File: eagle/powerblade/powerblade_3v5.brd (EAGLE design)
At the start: 25.4 x 25.4 mm, 78 parts, among them J1 JTAG_14PIN_IDC-ND, J2 AC_INFINAL, J4 TC2030-JLINK-NL, Q1 NTS4173, Q4 2SK1829, U1 TPS62122, U2 MCP6V3, U3 MSP430FR5738, U4 NRF51822QF, U6 MAX9910, U7 OPA2369, X1 16MHz, X3 32.768kHz, Y1 UREACH_XTEND

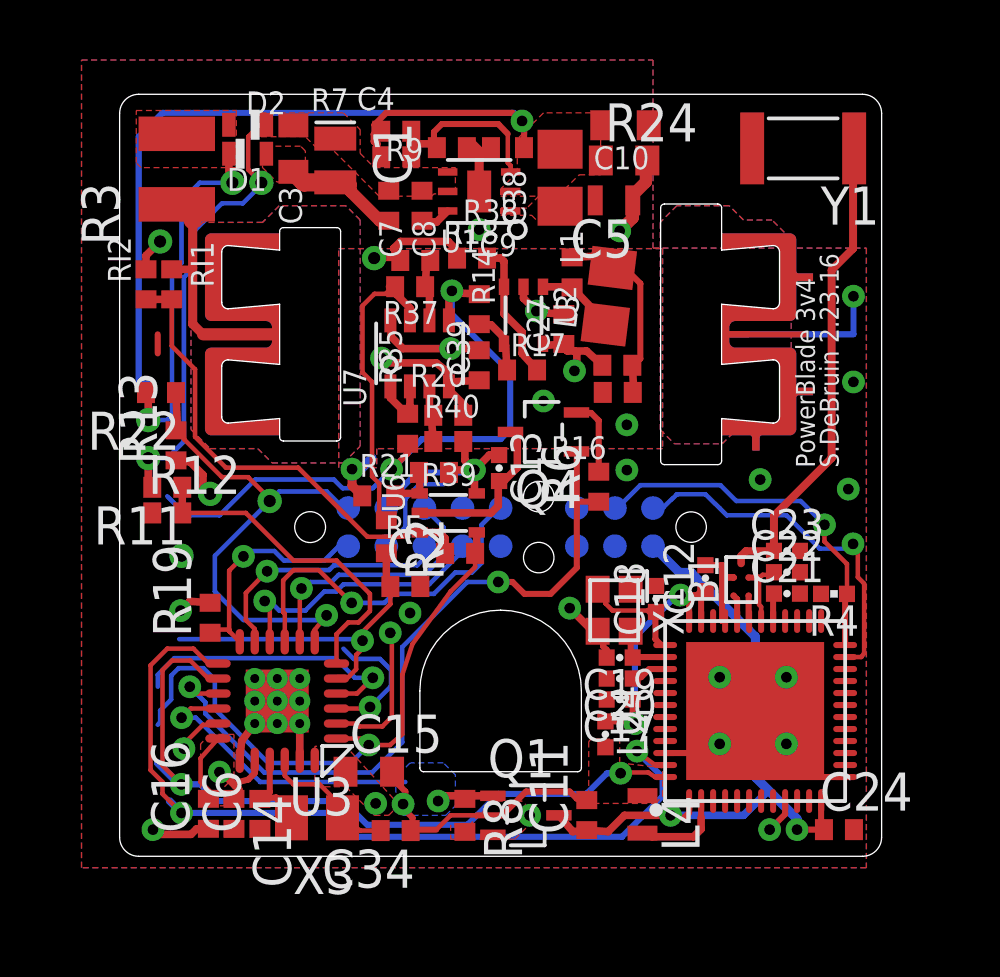
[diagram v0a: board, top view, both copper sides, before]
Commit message: cleaned up after removing header
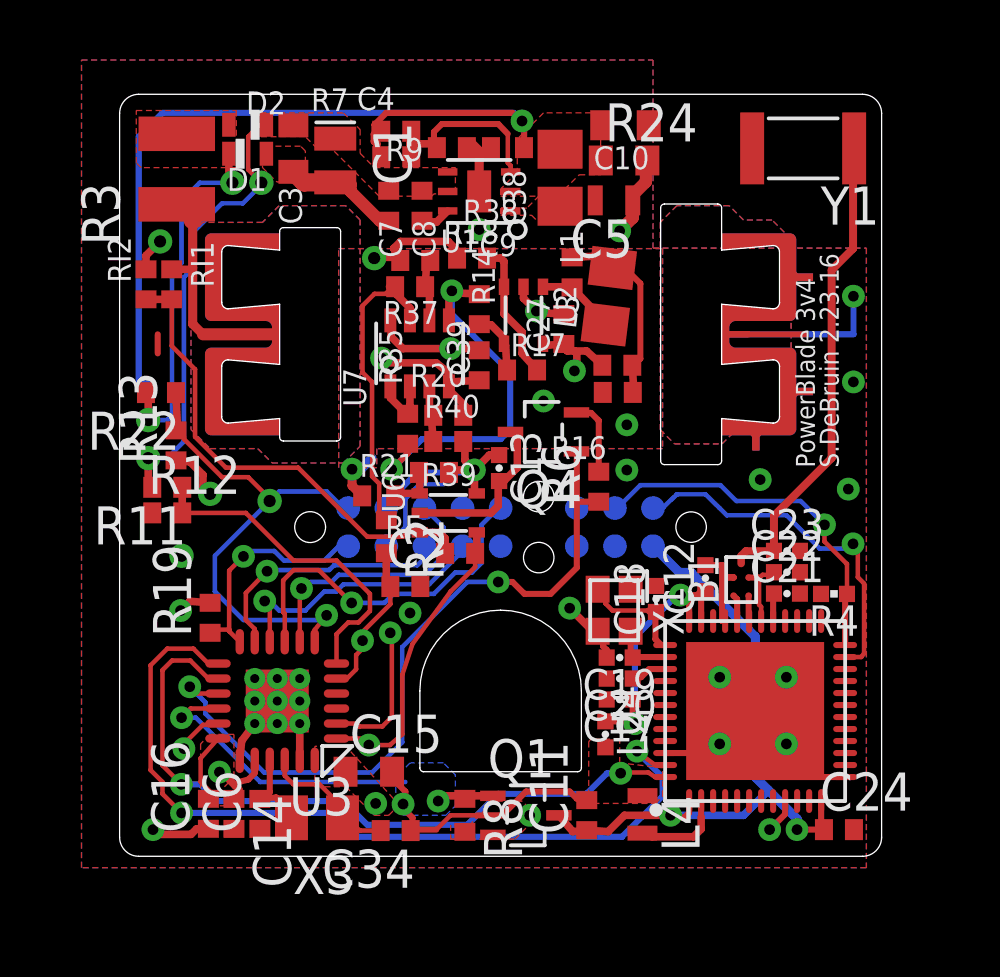
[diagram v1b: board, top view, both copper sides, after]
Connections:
- removed net PWM_CURRENT: U3.P3
- removed net PWM_VOLTAGE: U3.P4
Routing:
- net V_SENSE: track 20.6 -> 9.98 mm
- net PWM_VOLTAGE: track 9.49 -> 0.00 mm, vias 1 -> 0
- net VFILT: track 32.0 -> 23.4 mm
- net I_SENSE: track 11.3 -> 5.18 mm
- net PWM_CURRENT: track 4.54 -> 0.00 mm, vias 1 -> 0
- net FROMBLE_RX: track 24.8 -> 23.8 mm
- net TOBLE_TX: track 28.7 -> 28.1 mm
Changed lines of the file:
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@@
 <grid distance="25" unitdist="mil" unit="mil" style="lines" multiple="1" display="no" altdistance="3.125" altunitdist="mil" altunit="mil"/>
 <layers>
-<layer number="1" name="Top" color="4" fill="1" visible="yes" active="yes"/>
-<layer number="2" name="Route2" color="1" fill="3" visible="yes" active="yes"/>
+<layer number="1" name="Top" color="4" fill="1" visible="no" active="yes"/>
+<layer number="2" name="Route2" color="1" fill="3" visible="no" active="yes"/>
 <layer number="3" name="Route3" color="4" fill="3" visible="no" active="no"/>
 <layer number="4" name="Route4" color="1" fill="4" visible="no" active="no"/>
@@
 <layer number="13" name="Route13" color="4" fill="5" visible="no" active="no"/>
 <layer number="14" name="Route14" color="1" fill="6" visible="no" active="no"/>
-<layer number="15" name="Route15" color="4" fill="6" visible="yes" active="yes"/>
+<layer number="15" name="Route15" color="4" fill="6" visible="no" active="yes"/>
 <layer number="16" name="Bottom" color="1" fill="1" visible="yes" active="yes"/>
 <layer number="17" name="Pads" color="2" fill="1" visible="yes" active="yes"/>
@@
 <contactref element="RF" pad="2"/>
 <contactref element="U6" pad="P4"/>
-<wire x1="-11.43" y1="-13.0175" x2="-11.350625" y2="-12.938125" width="0.1524" layer="16"/>
-<wire x1="-11.350625" y1="-12.938125" x2="-11.350625" y2="-12.54125" width="0.1524" layer="16"/>
-<wire x1="-11.350625" y1="-12.54125" x2="-10.982325" y2="-12.17295" width="0.1524" layer="16"/>
-<wire x1="-10.982325" y1="-12.17295" x2="-10.982325" y2="-11.3792" width="0.1524" layer="16"/>
-<wire x1="-10.982325" y1="-11.3792" x2="-10.7299125" y2="-11.1267875" width="0.1524" layer="16"/>
 <via x="-4.3942" y="-13.69186875" extent="1-16" drill="0.3556"/>
-<wire x1="-4.3942" y1="-13.69186875" x2="-5.000625" y2="-14.2875" width="0.1524" layer="16"/>
-<wire x1="-5.000625" y1="-14.2875" x2="-7.750175" y2="-14.2875" width="0.1524" layer="16"/>
-<wire x1="-7.750175" y1="-14.2875" x2="-9.525" y2="-12.487275" width="0.1524" layer="16"/>
-<wire x1="-9.525" y1="-12.487275" x2="-9.525" y2="-11.509375" width="0.1524" layer="16"/>
-<wire x1="-9.525" y1="-11.509375" x2="-9.9075875" y2="-11.1267875" width="0.1524" layer="16"/>
-<wire x1="-9.9075875" y1="-11.1267875" x2="-10.7299125" y2="-11.1267875" width="0.1524" layer="16"/>
 <wire x1="-3.69061875" y1="-13.69186875" x2="-3.279775" y2="-13.335" width="0.1524" layer="1"/>
 <wire x1="-3.279775" y1="-13.335" x2="-3.279775" y2="-11.350625" width="0.1524" layer="1"/>
@@
 <wire x1="-3.0988" y1="-3.96875" x2="-3.6322" y2="-4.50215" width="0.2032" layer="1"/>
 <wire x1="-3.609975" y1="-4.524375" x2="-3.6322" y2="-4.50215" width="0.1524" layer="1"/>
-<wire x1="-3.6322" y1="-4.50215" x2="-4.26085" y2="-5.1308" width="0.1524" layer="16"/>
-<wire x1="-8.175625" y1="-4.841875" x2="-9.36625" y2="-6.0325" width="0.1524" layer="16"/>
-<wire x1="-9.36625" y1="-6.0325" x2="-10.4775" y2="-6.0325" width="0.1524" layer="16"/>
-<wire x1="-10.4775" y1="-6.0325" x2="-11.1125" y2="-5.3975" width="0.1524" layer="16"/>
-<wire x1="-4.26085" y1="-5.1308" x2="-5.267325" y2="-5.1308" width="0.1524" layer="16"/>
-<wire x1="-5.267325" y1="-5.1308" x2="-5.55625" y2="-4.841875" width="0.1524" layer="16"/>
-<wire x1="-5.55625" y1="-4.841875" x2="-8.175625" y2="-4.841875" width="0.1524" layer="16"/>
 <via x="-3.679825" y="-9.95045" extent="1-16" drill="0.3556"/>
 <contactref element="U3" pad="P2"/>
@@
 <wire x1="-4.816475" y1="-10.690225" x2="-4.60375" y2="-10.4775" width="0.1524" layer="1"/>
 <wire x1="-4.60375" y1="-10.4775" x2="-4.60375" y2="-10.2108" width="0.1524" layer="1"/>
-<wire x1="-10.715625" y1="-10.16" x2="-4.65455" y2="-10.16" width="0.1524" layer="16"/>
-<wire x1="-4.65455" y1="-10.16" x2="-4.60375" y2="-10.2108" width="0.1524" layer="16"/>
 <wire x1="-3.675" y1="-8.4074" x2="-3.675" y2="-8.993125" width="0.1524" layer="1"/>
 <wire x1="-3.675" y1="-8.993125" x2="-4.60375" y2="-9.921875" width="0.1524" layer="1"/>
@@
 <wire x1="4.524375" y1="-13.890625" x2="4.549775" y2="-13.890625" width="0.2032" layer="1"/>
 <wire x1="4.549775" y1="-13.890625" x2="4.5466" y2="-13.8938" width="0.2032" layer="1"/>
-<wire x1="-11.033125" y1="-15.5575" x2="-10.63625" y2="-15.954375" width="0.254" layer="16"/>
 <wire x1="-9.420375" y1="-10.97375" x2="-9.743125" y2="-10.97375" width="0.1524" layer="1"/>
 <wire x1="-9.743125" y1="-10.97375" x2="-10.239375" y2="-10.4775" width="0.1524" layer="1"/>
@@
 <via x="-10.6426" y="-15.001875" extent="1-16" drill="0.3556"/>
 <wire x1="-11.27125" y1="-14.366875" x2="-10.6426" y2="-15.001875" width="0.1524" layer="1"/>
-<wire x1="-11.43" y1="-14.2875" x2="-10.795" y2="-14.9225" width="0.254" layer="16"/>
-<wire x1="-10.795" y1="-14.9225" x2="-10.715625" y2="-14.9225" width="0.254" layer="16"/>
-<wire x1="-10.715625" y1="-14.9225" x2="-10.6426" y2="-15.001875" width="0.254" layer="16"/>
 <wire x1="-9.420375" y1="-11.47375" x2="-9.744775" y2="-11.47375" width="0.1524" layer="1"/>
 <wire x1="-9.744775" y1="-11.47375" x2="-10.34415" y2="-10.874375" width="0.1524" layer="1"/>
@@
 <wire x1="-12.065" y1="-1.508125" x2="-11.668125" y2="-1.666875" width="0.2032" layer="16"/>
 </signal>
-<signal name="PWM_CURRENT">
-<contactref element="U3" pad="P3"/>
-<via x="-4.352925" y="-12.423775" extent="1-16" drill="0.3556"/>
-<wire x1="-5.470375" y1="-12.47375" x2="-4.4029" y2="-12.47375" width="0.1524" layer="1"/>
-<wire x1="-4.022725" y1="-10.8204" x2="-4.89585" y2="-10.8204" width="0.1524" layer="16"/>
-<wire x1="-4.89585" y1="-10.8204" x2="-5.23875" y2="-10.4775" width="0.1524" layer="16"/>
-<wire x1="-4.4029" y1="-12.47375" x2="-4.352925" y2="-12.423775" width="0.1524" layer="1"/>
-<wire x1="-4.352925" y1="-12.423775" x2="-3.65125" y2="-11.7221" width="0.1524" layer="16"/>
-<wire x1="-3.65125" y1="-11.7221" x2="-3.65125" y2="-11.191875" width="0.1524" layer="16"/>
-<wire x1="-3.65125" y1="-11.191875" x2="-4.022725" y2="-10.8204" width="0.1524" layer="16"/>
-</signal>
-<signal name="PWM_VOLTAGE">
-<contactref element="U3" pad="P4"/>
-<via x="-4.26085" y="-11.44905" extent="1-16" drill="0.3556"/>
-<wire x1="-11.43" y1="-11.7475" x2="-11.43" y2="-11.350625" width="0.1524" layer="16"/>
-<wire x1="-11.43" y1="-11.350625" x2="-10.874375" y2="-10.795" width="0.1524" layer="16"/>
-<wire x1="-5.5118" y1="-10.795" x2="-10.874375" y2="-10.795" width="0.1524" layer="16"/>
-<wire x1="-5.470375" y1="-11.97375" x2="-4.78555" y2="-11.97375" width="0.1524" layer="1"/>
-<wire x1="-4.78555" y1="-11.97375" x2="-4.26085" y2="-11.44905" width="0.1524" layer="1"/>
-<wire x1="-5.5118" y1="-10.795" x2="-4.85775" y2="-11.44905" width="0.1524" layer="16"/>
-<wire x1="-4.85775" y1="-11.44905" x2="-4.26085" y2="-11.44905" width="0.1524" layer="16"/>
-</signal>
 <signal name="N$10">
